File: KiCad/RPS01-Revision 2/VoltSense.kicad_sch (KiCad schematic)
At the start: 12 parts, among them U20 UA741CDT, U21 UA741CDT

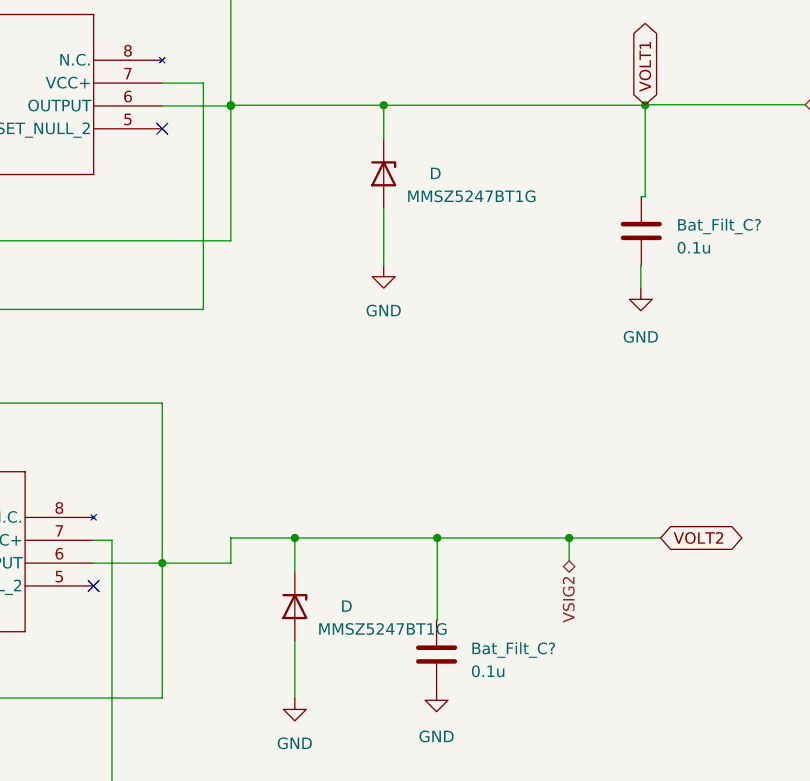
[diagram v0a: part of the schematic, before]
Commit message: Reduced the References for Peter
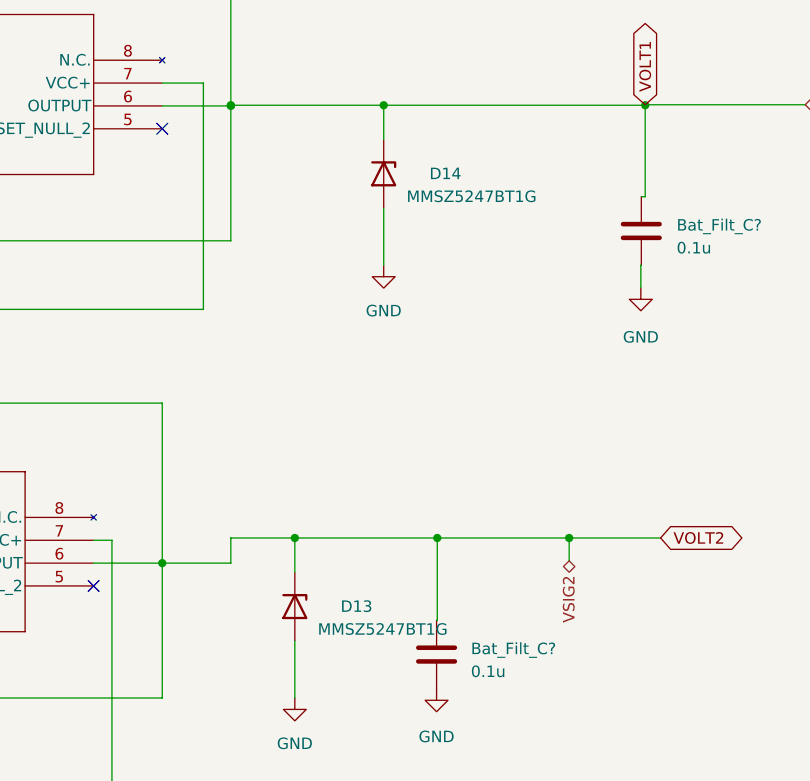
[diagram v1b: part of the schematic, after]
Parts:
- renumbered D to D13, D to D14
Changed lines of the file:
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@@
         )
         (path "/14930f15-c0a0-4b55-93e6-b112548415f6/86aa0a4b-8e23-451d-9b8a-c1446d1d5d38"
-          (reference "R") (unit 1)
+          (reference "R47") (unit 1)
         )
       )
@@
   (symbol (lib_id "Device:D_Zener") (at 139.192 92.202 270) (unit 1)
     (in_bom yes) (on_board yes) (dnp no)
-    (property "Reference" "D" (at 144.272 92.202 90)
+    (property "Reference" "D13" (at 144.272 92.202 90)
       (effects (font (size 1.27 1.27)) (justify left))
     )
@@
       (project "rps01"
         (path "/14930f15-c0a0-4b55-93e6-b112548415f6/86aa0a4b-8e23-451d-9b8a-c1446d1d5d38"
-          (reference "D") (unit 1)
+          (reference "D13") (unit 1)
         )
       )
@@
         )
         (path "/14930f15-c0a0-4b55-93e6-b112548415f6/86aa0a4b-8e23-451d-9b8a-c1446d1d5d38"
-          (reference "R") (unit 1)
+          (reference "R50") (unit 1)
         )
       )
@@
         )
         (path "/14930f15-c0a0-4b55-93e6-b112548415f6/86aa0a4b-8e23-451d-9b8a-c1446d1d5d38"
-          (reference "R") (unit 1)
+          (reference "R46") (unit 1)
         )
       )
@@
         )
         (path "/14930f15-c0a0-4b55-93e6-b112548415f6/86aa0a4b-8e23-451d-9b8a-c1446d1d5d38"
-          (reference "R") (unit 1)
+          (reference "R49") (unit 1)
         )
       )
@@
   (symbol (lib_id "Device:D_Zener") (at 149.0665 44.1201 270) (unit 1)
     (in_bom yes) (on_board yes) (dnp no)
-    (property "Reference" "D" (at 154.1465 44.1201 90)
+    (property "Reference" "D14" (at 154.1465 44.1201 90)
       (effects (font (size 1.27 1.27)) (justify left))
     )
@@
       (project "rps01"
         (path "/14930f15-c0a0-4b55-93e6-b112548415f6/86aa0a4b-8e23-451d-9b8a-c1446d1d5d38"
-          (reference "D") (unit 1)
+          (reference "D14") (unit 1)
         )
       )
@@
         )
         (path "/14930f15-c0a0-4b55-93e6-b112548415f6/86aa0a4b-8e23-451d-9b8a-c1446d1d5d38"
-          (reference "C") (unit 1)
+          (reference "C39") (unit 1)
         )
       )
@@
         )
         (path "/14930f15-c0a0-4b55-93e6-b112548415f6/86aa0a4b-8e23-451d-9b8a-c1446d1d5d38"
-          (reference "C") (unit 1)
+          (reference "C40") (unit 1)
         )
       )
@@
         )
         (path "/14930f15-c0a0-4b55-93e6-b112548415f6/86aa0a4b-8e23-451d-9b8a-c1446d1d5d38"
-          (reference "R") (unit 1)
+          (reference "R45") (unit 1)
         )
       )
@@
         )
         (path "/14930f15-c0a0-4b55-93e6-b112548415f6/86aa0a4b-8e23-451d-9b8a-c1446d1d5d38"
-          (reference "R") (unit 1)
-        )
-      )
+          (reference "R48") (unit 1)
+        )
+      )
